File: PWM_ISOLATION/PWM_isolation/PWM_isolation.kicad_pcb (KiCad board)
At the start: 2 copper layers, 90 x 80 mm, 53 parts, among them J1 Conn_01x02_Socket, J10 XT60_Male, J11 Conn_01x03_Pin, J12 Conn_01x02_Socket, J2 Conn_01x02_Socket, J3 Conn_01x02_Socket, J4 Conn_01x02_Socket, J5 Conn_01x05_Socket, J6 Conn_01x03_Socket, J7 Conn_01x03_Socket, J8 Conn_01x03_Socket, J9 Conn_01x03_Socket, U1 TBD62783A, U2 LTV-847, U3 NJM317F

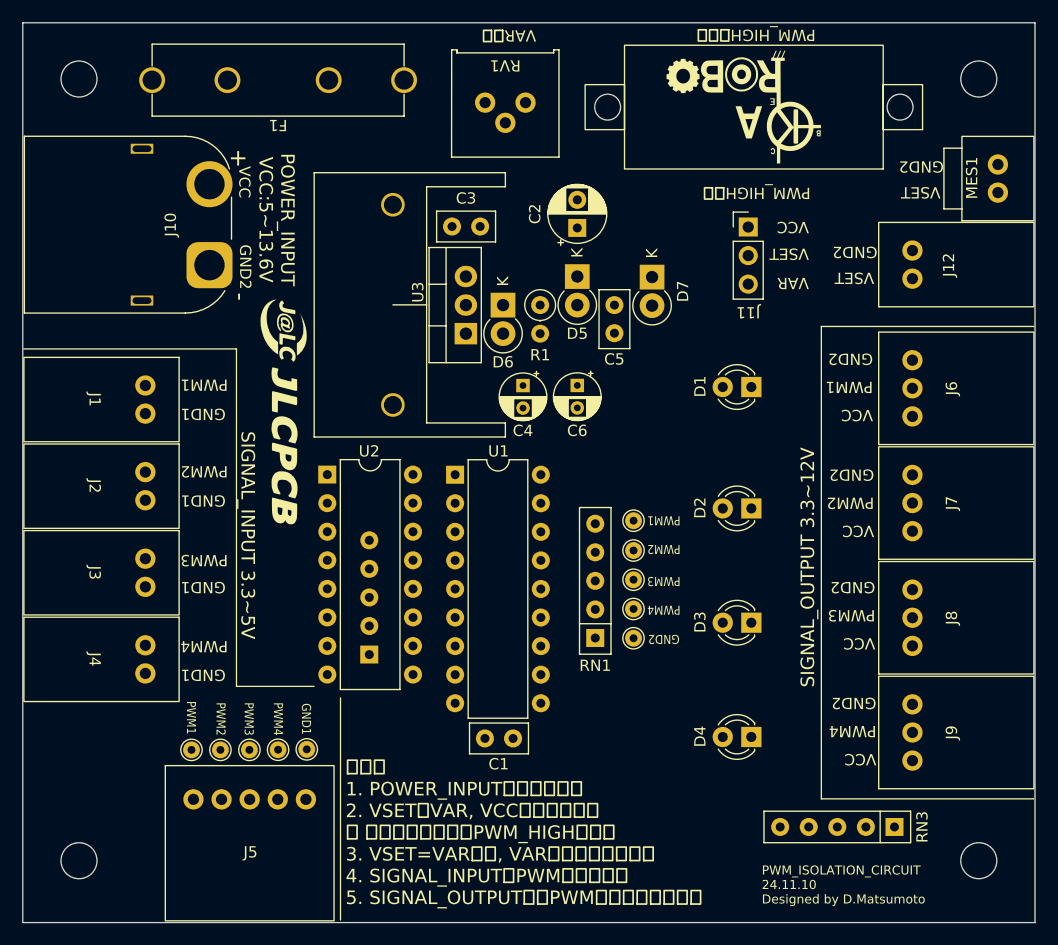
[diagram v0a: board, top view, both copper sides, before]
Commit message: UPDATE_PWM_ISOLATION
PWM絶縁回路のPCBデータを修正
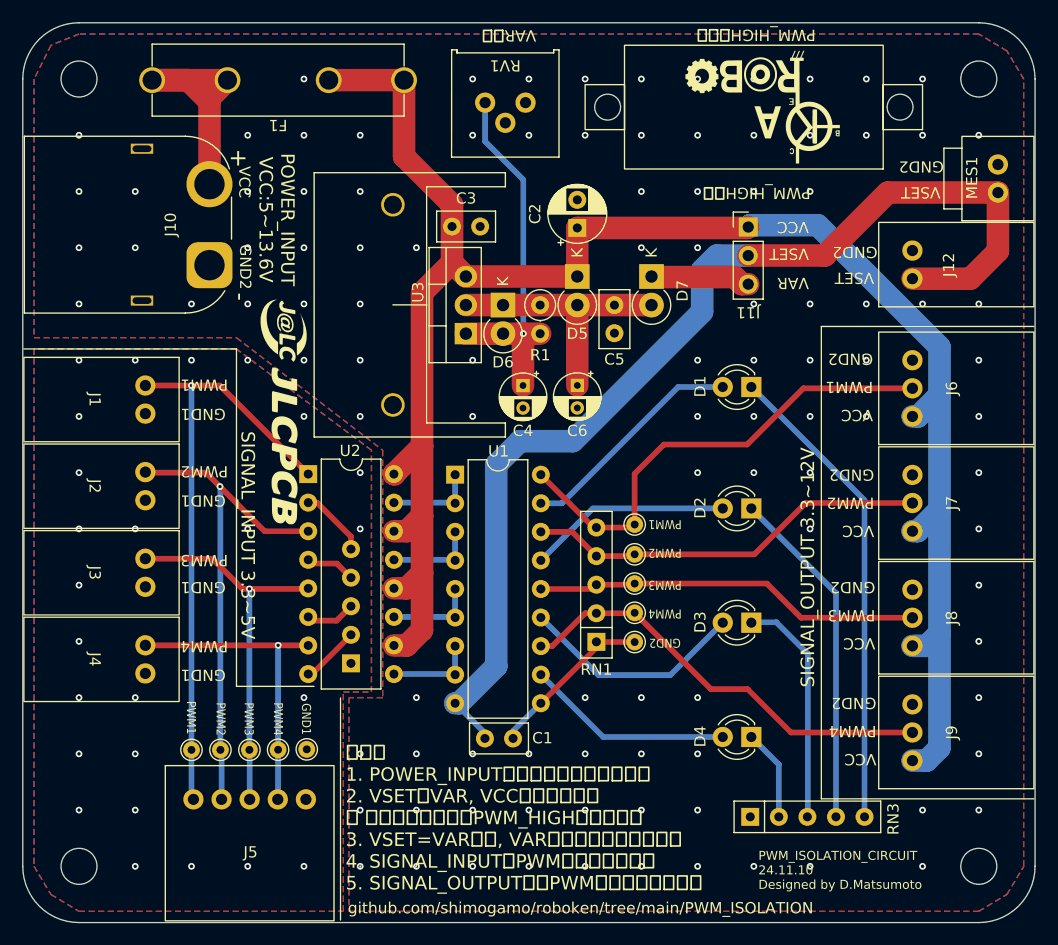
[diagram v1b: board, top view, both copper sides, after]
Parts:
- moved RN3 12.9 mm to (164.7, 120.6), turned to 0 degrees
- moved RN2 1.81 mm to (129.2, 107.0)
- moved U2 1.70 mm to (125.4, 90.1)
- moved G*** 1.68 mm to (166.0, 57.5)
- moved REF** 0.50 mm to (185.0, 125.0)
- moved REF** 0.50 mm to (105.0, 125.0)
- moved RN1 0.35 mm to (151.0, 105.0)
- moved TP1 0.35 mm to (154.4, 94.6)
- moved TP2 0.35 mm to (154.4, 97.3)
- moved TP3 0.35 mm to (154.4, 99.9)
- moved TP6 0.35 mm to (154.4, 105.1)
- moved TP5 0.35 mm to (154.4, 102.5)
- moved D7 0.07 mm to (155.9, 72.6)
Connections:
- J10 pad 1: Net-(J10-Pin_1) -> GND2
- J10 pad 2: GND2 -> Net-(J10-Pin_1)
- MES1 pad 1: GND2 -> VSET
- MES1 pad 2: VSET -> GND2
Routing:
- net VCC: track 0.00 -> 171.8 mm
- net VSET: track 0.00 -> 97.8 mm
- net PWM1: track 0.00 -> 54.6 mm, vias 0 -> 1
- net PWM2: track 0.00 -> 44.5 mm, vias 0 -> 1
- net Net-(J6-Pin_2): track 0.00 -> 42.8 mm
- net Net-(D1-K): track 0.00 -> 42.4 mm
- net Net-(J9-Pin_2): track 0.00 -> 38.7 mm
- net Net-(J7-Pin_2): track 0.00 -> 35.9 mm
- net Net-(J8-Pin_2): track 0.00 -> 34.5 mm
- net PWM3: track 0.00 -> 34.4 mm, vias 0 -> 1
- net Net-(D6-A): track 0.00 -> 33.2 mm, vias 0 -> 1
- net Net-(D2-K): track 0.00 -> 30.5 mm
- net PWM4: track 0.00 -> 28.2 mm, vias 0 -> 1
- net /可変三端子レギュレータ/VARIABLE: track 0.00 -> 23.7 mm
- net Net-(J10-Pin_1): track 0.00 -> 22.5 mm
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- added copper zone on B.Cu, net GND1
- added copper zone on F.Cu, net GND1
- added copper zone on B.Cu, net GND2
- added copper zone on F.Cu, net GND2
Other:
- outline, holes or cut-outs redrawn
- board text added: "github.com/shimogamo/roboken/tree/main/PWM_ISOLATION"
- board text added: "使い方 1. POWER_INPUTにモータ駆動電源を接続 2. VSETをVAR, VCCのいずれかと ジャンパで接続しPWM_HIGHを設定する 3. VSET=VARなら, VARを可変抵抗で調整する 4. SIGNAL_INPUTにPWM信号を入力する 5. SIGNAL_OUTPUTからPWM信号が出力される"
- board text removed: "使い方 1. POWER_INPUTに電源を接続 2. VSETをVAR, VCCのいずれかと ジャンパで接続しPWM_HIGHを設定 3. VSET=VARなら, VARを可変抵抗で調整 4. SIGNAL_INPUTにPWM信号を入力 5. SIGNAL_OUTPUTからPWM信号が出力される"

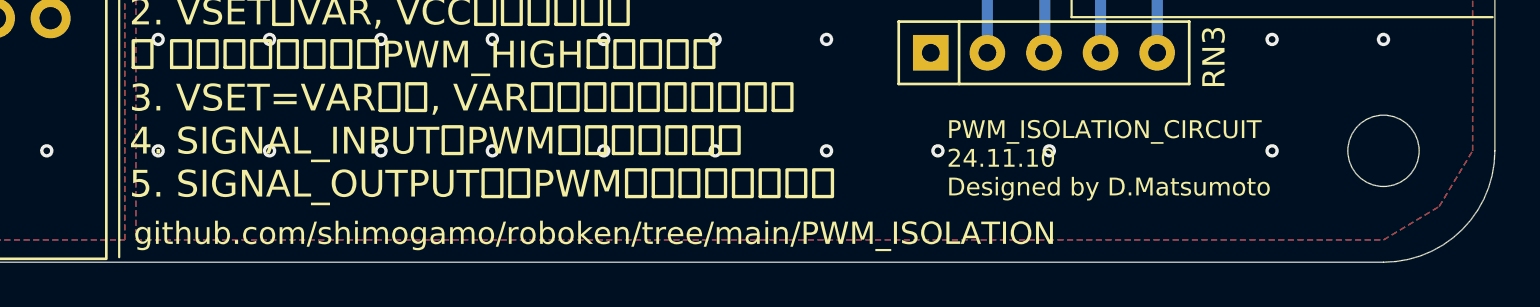
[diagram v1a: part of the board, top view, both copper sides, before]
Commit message: CREATE gerber file for PWM_ISOLATION_CIRCUIT
PWM_ISOLATION_CIRCUITのガーバーファイルを作成
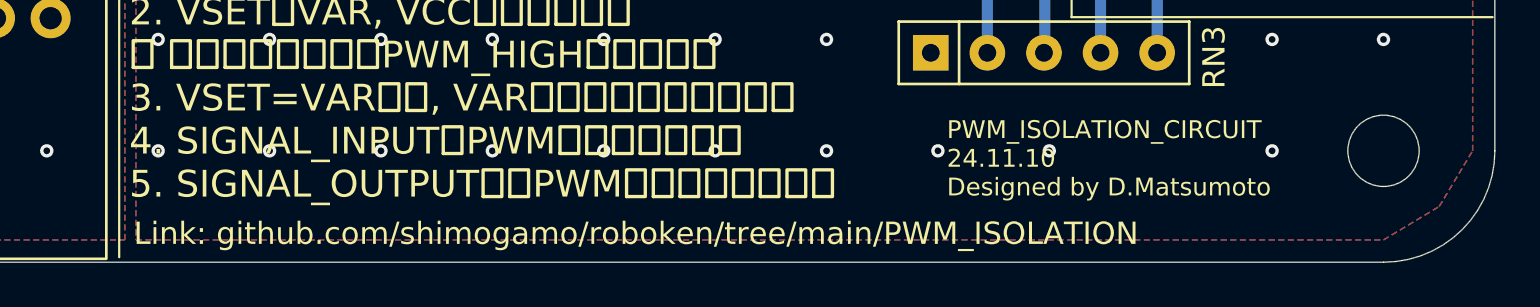
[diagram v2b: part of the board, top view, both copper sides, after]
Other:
- board text added: "Link: github.com/shimogamo/roboken/tree/main/PWM_ISOLATION"
- board text removed: "github.com/shimogamo/roboken/tree/main/PWM_ISOLATION"
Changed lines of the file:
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@@
 		(pad_to_mask_clearance 0)
 		(allow_soldermask_bridges_in_footprints no)
+		(aux_axis_origin 100 50)
 		(pcbplotparams
 			(layerselection 0x00010fc_ffffffff)
@@
 			(outputformat 1)
 			(mirror no)
-			(drillshape 1)
+			(drillshape 0)
 			(scaleselection 1)
-			(outputdirectory "")
+			(outputdirectory "Gerber")
 		)
 	)
@@
 		)
 		(property "Value" "330~1k"
-			(at 6.35 2.4 360)
+			(at 6.35 2.4 0)
 			(layer "F.Fab")
 			(effects
@@
 		)
 		(fp_text user "${REFERENCE}"
-			(at 5.08 0 360)
+			(at 5.08 0 0)
 			(layer "F.Fab")
 			(effects
@@
 		)
 	)
-	(gr_text "github.com/shimogamo/roboken/tree/main/PWM_ISOLATION"
+	(gr_text "Link: github.com/shimogamo/roboken/tree/main/PWM_ISOLATION"
 		(at 128.9 129.3 0)
 		(layer "F.SilkS")
